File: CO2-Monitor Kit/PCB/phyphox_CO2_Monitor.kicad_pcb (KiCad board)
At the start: 2 copper layers, 73.1 x 42 mm, 17 parts, among them J1 Conn_01x19_Female, J2 Conn_01x19_Female, J3 Conn_01x07_Male, U1 ESP32-DEVKITC-32D, U2 SCD30

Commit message: Update CO2 Monitor Kit Rev 0.7
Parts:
- removed J3: Conn_01x07_Male, Connector_PinHeader_2.54mm:PinHeader_1x07_P2.54mm_Vertical
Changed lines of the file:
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@@
-(kicad_pcb (version 20171130) (host pcbnew "(5.1.2)-1")
+(kicad_pcb (version 20171130) (host pcbnew "(5.1.0)-1")
   (general
     (thickness 1.6)
@@
     (tracks 74)
     (zones 0)
-    (modules 17)
+    (modules 16)
     (nets 43)
   )
@@
       (outputformat 1)
       (mirror false)
-      (drillshape 1)
+      (drillshape 0)
       (scaleselection 1)
-      (outputdirectory ""))
+      (outputdirectory "manufacturing_files"))
   )
   (net 0 "")
@@
       (net 27 "Net-(J2-Pad19)"))
   )
-  (module Connector_PinHeader_2.54mm:PinHeader_1x07_P2.54mm_Vertical (layer B.Cu)
-    (at 190.7348 94.9232)
-    (descr "Through hole straight pin header, 1x07, 2.54mm pitch, single row")
-    (tags "Through hole pin header THT 1x07 2.54mm single row")
-    (fp_text reference J3 (at 0 2.33) (layer B.SilkS)
-      (effects (font (size 1 1) (thickness 0.15)) (justify mirror))
-    )
-    (fp_text value Conn_01x07_Male (at -0.57 -17.81) (layer B.Fab) hide
-      (effects (font (size 1 1) (thickness 0.15)) (justify mirror))
-    )
-    (fp_line (start -0.635 1.27) (end 1.27 1.27) (layer B.Fab) (width 0.1))
-    (fp_line (start 1.27 1.27) (end 1.27 -16.51) (layer B.Fab) (width 0.1))
-    (fp_line (start 1.27 -16.51) (end -1.27 -16.51) (layer B.Fab) (width 0.1))
-    (fp_line (start -1.27 -16.51) (end -1.27 0.635) (layer B.Fab) (width 0.1))
-    (fp_line (start -1.27 0.635) (end -0.635 1.27) (layer B.Fab) (width 0.1))
-    (fp_line (start -1.33 -16.57) (end 1.33 -16.57) (layer B.SilkS) (width 0.12))
-    (fp_line (start -1.33 -1.27) (end -1.33 -16.57) (layer B.SilkS) (width 0.12))
-    (fp_line (start 1.33 -1.27) (end 1.33 -16.57) (layer B.SilkS) (width 0.12))
-    (fp_line (start -1.33 -1.27) (end 1.33 -1.27) (layer B.SilkS) (width 0.12))
-    (fp_line (start -1.33 0) (end -1.33 1.33) (layer B.SilkS) (width 0.12))
-    (fp_line (start -1.33 1.33) (end 0 1.33) (layer B.SilkS) (width 0.12))
-    (fp_line (start -1.8 1.8) (end -1.8 -17.05) (layer B.CrtYd) (width 0.05))
-    (fp_line (start -1.8 -17.05) (end 1.8 -17.05) (layer B.CrtYd) (width 0.05))
-    (fp_line (start 1.8 -17.05) (end 1.8 1.8) (layer B.CrtYd) (width 0.05))
-    (fp_line (start 1.8 1.8) (end -1.8 1.8) (layer B.CrtYd) (width 0.05))
-    (fp_text user %R (at 0 -7.62 -90) (layer B.Fab)
-      (effects (font (size 1 1) (thickness 0.15)) (justify mirror))
-    )
-    (pad 7 thru_hole oval (at 0 -15.24) (size 1.7 1.7) (drill 1) (layers *.Cu *.Mask)
-      (net 8 GND))
-    (pad 6 thru_hole oval (at 0 -12.7) (size 1.7 1.7) (drill 1) (layers *.Cu *.Mask)
-      (net 42 "Net-(J3-Pad6)"))
-    (pad 5 thru_hole oval (at 0 -10.16) (size 1.7 1.7) (drill 1) (layers *.Cu *.Mask)
-      (net 7 RDY))
-    (pad 4 thru_hole oval (at 0 -7.62) (size 1.7 1.7) (drill 1) (layers *.Cu *.Mask)
-      (net 5 SDA))
-    (pad 3 thru_hole oval (at 0 -5.08) (size 1.7 1.7) (drill 1) (layers *.Cu *.Mask)
-      (net 6 SCL))
-    (pad 2 thru_hole oval (at 0 -2.54) (size 1.7 1.7) (drill 1) (layers *.Cu *.Mask)
-      (net 8 GND))
-    (pad 1 thru_hole rect (at 0 0) (size 1.7 1.7) (drill 1) (layers *.Cu *.Mask)
-      (net 2 VDD))
-    (model ${KISYS3DMOD}/Connector_PinHeader_2.54mm.3dshapes/PinHeader_1x07_P2.54mm_Vertical.wrl
-      (at (xyz 0 0 0))
-      (scale (xyz 1 1 1))
-      (rotate (xyz 0 0 0))
-    )
-  )
   (module Connector_PinSocket_2.54mm:PinSocket_1x19_P2.54mm_Vertical (layer F.Cu)

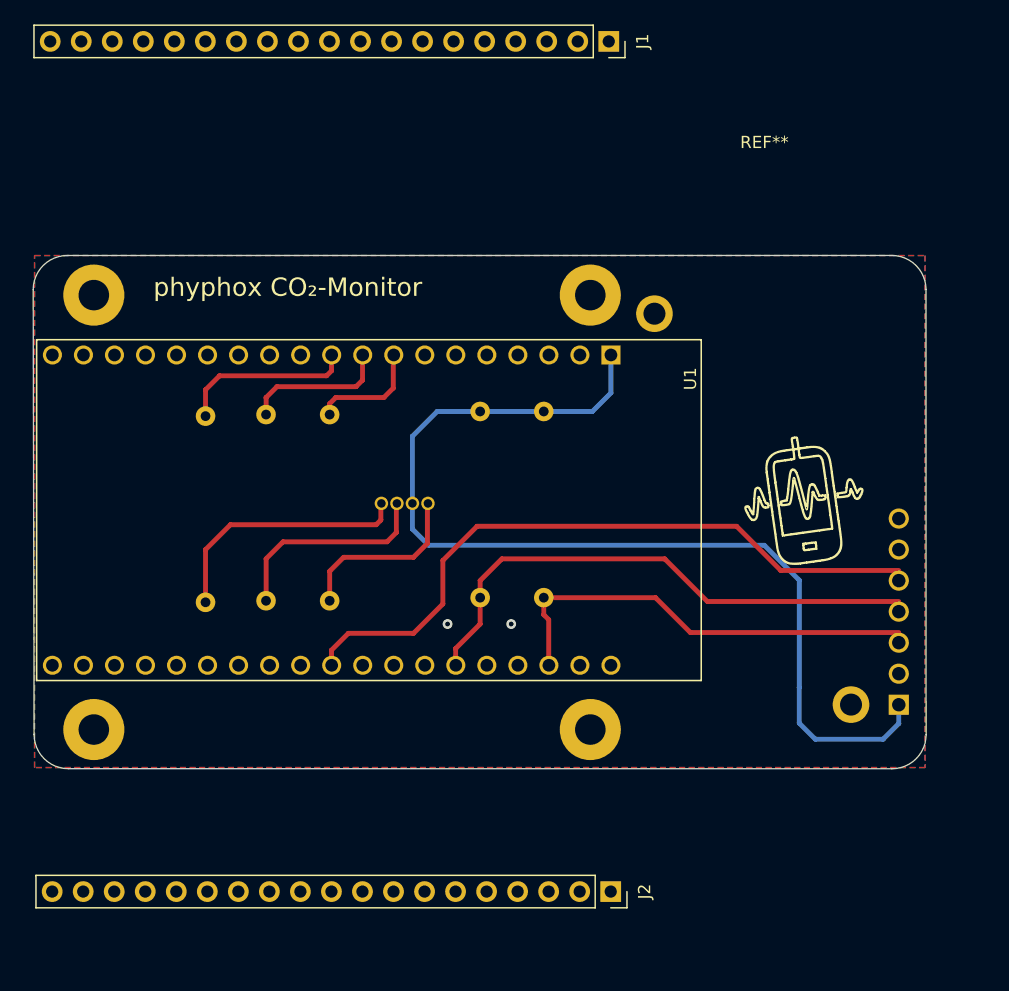
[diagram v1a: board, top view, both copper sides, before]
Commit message: [REV 1] Mounting Holes M2.5 -> M3, I2C port available
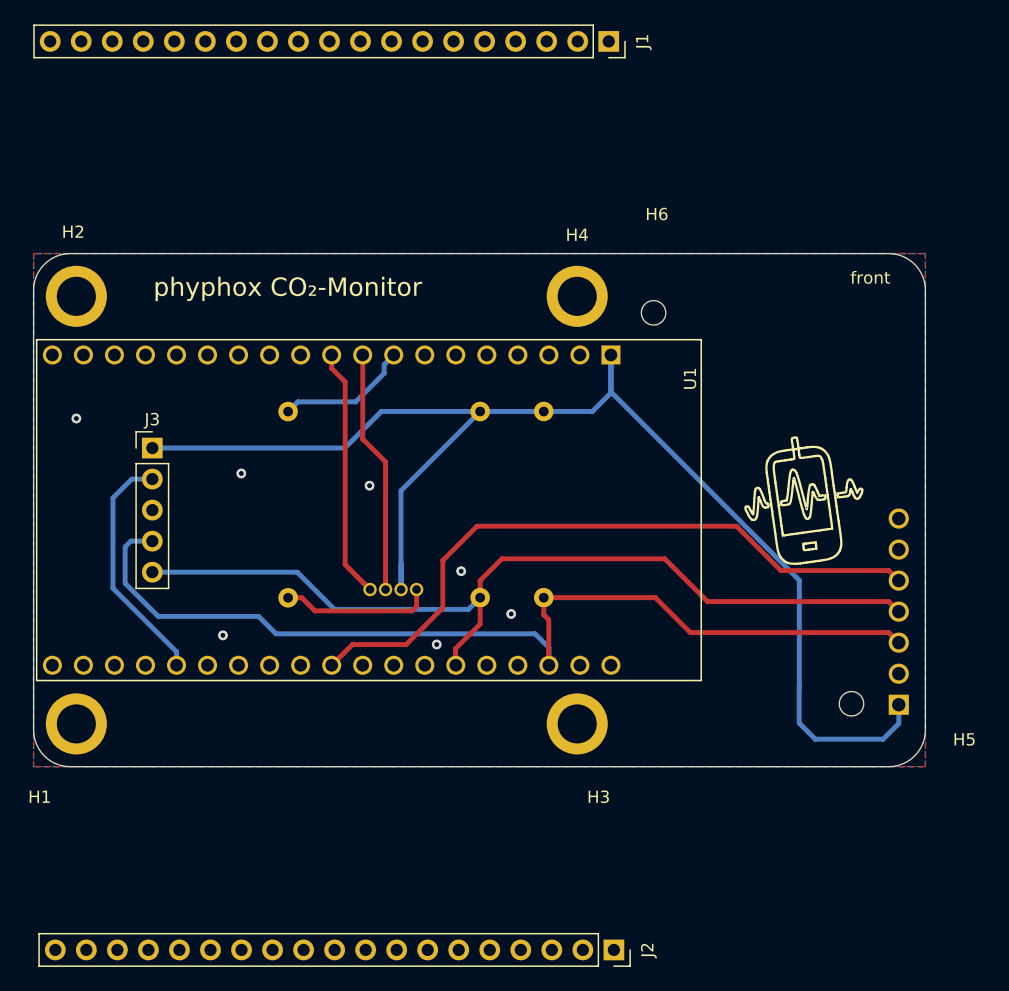
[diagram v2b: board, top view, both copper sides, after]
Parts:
- removed the R1 at (132.8, 86.1)
- removed the R3 at (138.0, 86.1)
- removed REF** (x2): MountingHole_2.2mm_M2_DIN965_Pad, MountingHole:MountingHole_2.2mm_M2_DIN965_Pad
- removed REF** (x4): MountingHole_2.5mm_Pad, MountingHole:MountingHole_2.5mm_Pad
- added H1: MountingHole, phyphox_CO2_Monitor:MountingHoleM3, F.Cu at (117.3, 96.2)
- added H2: MountingHole, phyphox_CO2_Monitor:MountingHoleM3, F.Cu at (117.3, 61.2)
- added H3: MountingHole, phyphox_CO2_Monitor:MountingHoleM3, F.Cu at (158.3, 96.2)
- added H4: MountingHole, phyphox_CO2_Monitor:MountingHoleM3, F.Cu at (158.3, 61.2)
- added H5: MountingHole, MountingHole:MountingHole_2mm, F.Cu at (180.7, 94.5)
- added H6: MountingHole, MountingHole:MountingHole_2mm, F.Cu at (164.5, 62.5)
- added J3: Conn_01x05_Female, Connector_PinHeader_2.54mm:PinHeader_1x05_P2.54mm_Vertical, F.Cu at (123.5, 73.6)
- R1: renamed from R2; value 1 -> 56
- moved D1 7.11 mm to (138.8, 85.2)
- moved R1 6.77 mm to (134.6, 85.9)
- moved J2 4.78 mm to (161.3, 114.7)
- renumbered R4 to R2, R5 to R3
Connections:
- net Net-(J2-Pad15) renamed ADC13GPIO15
- D1 pad 3: Net-(D1-Pad3) -> BLUE
- D1 pad 4: Net-(D1-Pad4) -> GREEN
- J1 pad 8: BLUE -> RED
- J1 pad 9: RED -> BLUE
- R1 pad 1: Net-(D1-Pad4) -> Net-(D1-Pad1)
- R1 pad 2: GREEN -> RED
- U1 pad 8: BLUE -> RED
- U1 pad 9: RED -> BLUE
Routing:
- net SCL: track 35.9 -> 80.0 mm
- net SDA: track 44.2 -> 73.0 mm
- net VDD: track 84.3 -> 109.2 mm
- net Net-(D1-Pad4): track 21.1 -> 0.00 mm
- net ADC13GPIO15: track 0.00 -> 19.7 mm
- net Net-(D1-Pad3): track 17.4 -> 0.00 mm
- net BLUE: track 9.38 -> 20.0 mm
- net GREEN: track 14.4 -> 20.5 mm
- net Net-(D1-Pad1): track 14.7 -> 12.5 mm
- net RED: track 12.0 -> 11.0 mm
- net GND: vias 2 -> 7
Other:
- board size 73.1 x 42 mm -> 73 x 42 mm
- board text added: "3.3V"
- board text added: "GND"
- board text added: "GPIO15"
- board text added: "Rev 1.0"
- board text added: "SCL"
- board text added: "SDA"
- board text added: "back"
- board text added: "front"
- board text removed: "Rev 0.7"

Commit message: [CO2Kit] Update manufacturing files
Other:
- board text added: "GPIO 2"
- board text removed: "GPIO15"
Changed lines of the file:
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@@
   (layers
     (0 F.Cu signal hide)
-    (31 B.Cu signal)
+    (31 B.Cu signal hide)
     (32 B.Adhes user)
     (33 F.Adhes user)
@@
       (outputformat 1)
       (mirror false)
-      (drillshape 1)
+      (drillshape 0)
       (scaleselection 1)
-      (outputdirectory ""))
+      (outputdirectory "manufacturing_files/"))
   )
   (net 0 "")
@@
     (effects (font (size 1 1) (thickness 0.15)) (justify mirror))
   )
-  (gr_text GPIO15 (at 119.0148 75.9492) (layer B.SilkS)
+  (gr_text "GPIO 2" (at 119.0148 75.9492) (layer B.SilkS)
     (effects (font (size 1 1) (thickness 0.15)) (justify mirror))
   )
